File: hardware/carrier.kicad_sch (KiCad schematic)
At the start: 49 parts, among them J2 Heltec_J2, J3 Heltec_J3, U1 MT3608

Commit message: hardware: gen_sch net classes load in KiCad 9, respect lib in_bom
KiCad 9 silently drops every net class whose JSON lacks "priority", so the
Power class never reached pcbnew/DRC. MountingHole symbols are in_bom=no in
the library; keep that so footprint/symbol BOM flags match (parity).

Co-Authored-By: Claude Opus 5.5 <noreply@anthropic.com>
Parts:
- H1, H2, H3, H4: now left out of the parts list
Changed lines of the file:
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@@
 		(unit 1)
 		(exclude_from_sim no)
-		(in_bom yes)
+		(in_bom no)
 		(on_board yes)
 		(dnp no)
@@
 		(unit 1)
 		(exclude_from_sim no)
-		(in_bom yes)
+		(in_bom no)
 		(on_board yes)
 		(dnp no)
@@
 		(unit 1)
 		(exclude_from_sim no)
-		(in_bom yes)
+		(in_bom no)
 		(on_board yes)
 		(dnp no)
@@
 		(unit 1)
 		(exclude_from_sim no)
-		(in_bom yes)
+		(in_bom no)
 		(on_board yes)
 		(dnp no)

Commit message: hardware: JLCPCB assembly BOM + CPL (full SMD+THT)
design.py: LCSC map keyed by (value, footprint); check() fails if an
assembled part (not DNP, not a mounting hole) has no LCSC number or an
entry is unused. Part numbers verified live against JLCPCB's parts API
on 2026-09-29. Cap values now state the picked parts' ratings:
22uF 25V, 220uF 16V, 100uF 25V.

jlc.py (run by make fab) writes fab/jlc_bom.csv and fab/jlc_cpl.csv from
design.py and kicad-cli's pos export, and checks: BOM and CPL designators
match exactly once, every row has an LCSC number, the pos anchors equal
the board coordinates with Y negated (the Gerber convention), and every
placement lies inside the Gerber Edge.Cuts extent. Mid X/Y is the pad
centre, because THT footprints are anchored on pin 1. No rotation
offsets: ORDERING.md lists the parts to check in JLC's 3D preview.

ORDERING.md: Economic PCBA section (upload steps, THT, setup-fee types,
preview checks, stock and backups).

Co-Authored-By: Claude Opus 5.5 <noreply@anthropic.com>
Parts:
- C_BULK1: value 220uF 10V -> 220uF 16V
- C_IN1, C_OUT1, C_OUT2: value 22uF 10V -> 22uF 25V
- C_NFC1: value 100uF 10V -> 100uF 25V
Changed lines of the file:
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@@
 			)
 		)
-		(property "Value" "22uF 10V"
+		(property "Value" "22uF 25V"
 			(at 153.035 101.6 0)
 			(effects
@@
 			)
 		)
-		(property "Value" "22uF 10V"
+		(property "Value" "22uF 25V"
 			(at 168.275 96.52 0)
 			(effects
@@
 			)
 		)
-		(property "Value" "22uF 10V"
+		(property "Value" "22uF 25V"
 			(at 183.515 96.52 0)
 			(effects
@@
 			)
 		)
-		(property "Value" "220uF 10V"
+		(property "Value" "220uF 16V"
 			(at 201.295 101.6 0)
 			(effects
@@
 			)
 		)
-		(property "Value" "100uF 10V"
+		(property "Value" "100uF 25V"
 			(at 33.655 142.24 0)
 			(effects

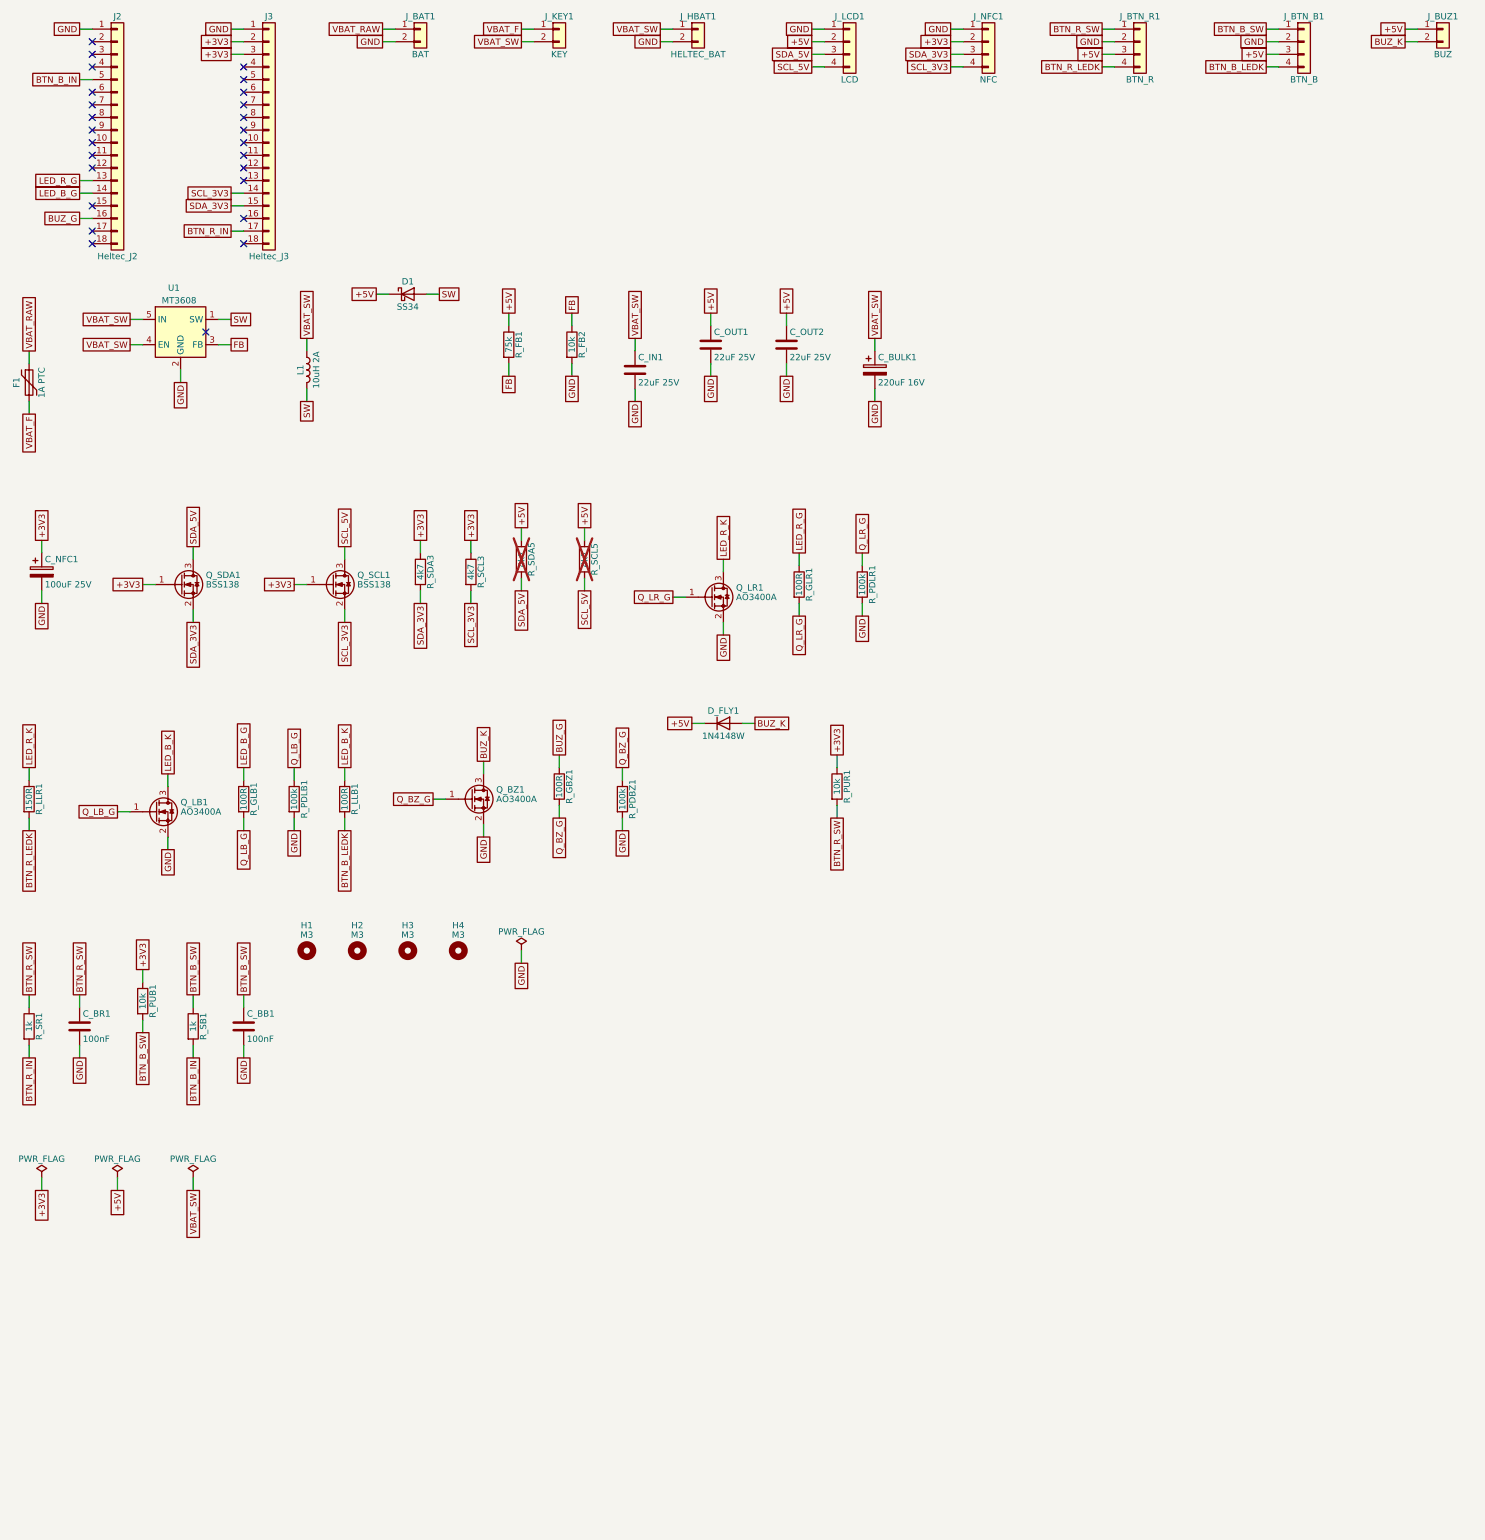
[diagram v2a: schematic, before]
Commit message: hardware: I2S speaker amp, TCA9534 expander, ceramic bulk caps
Task A10 (design Part 6):
- U2 TCA9534PWR (C783615) at 0x20 on the 3V3 I2C bus, INT on GPIO6
  (R_INT1 10k): buttons on P0/P1, LED/buzzer gate drives on P2-P4,
  amp SD_MODE on P5 (through R_SD1 1k, datasheet abs-max guidance).
- U3 MAX98357AETE+T (C910544) on VBAT_SW, I2S on GPIO47/48/21, 12 dB,
  BTL output to J_SPK1 (pin 1 OUT-, silk "SPK (BTL, not GND)").
- THT 220uF/100uF -> 2x 47uF 10V (C96123) + 100uF 6.3V (C15008) 1206
  Basic ceramics; F1 -> 2A PTC 1206L200/16NR (C22374899).
- R_LLR1/R_LLB1 -> 0R (C17477): ONPOW 6V button LEDs have a resistor.
- GND leaves the Power net class, Power clearance 0.2 mm, board min
  track 0.15 mm (Freerouting necks into the fine-pitch pads); U3
  thermal vias widened to 0.3 mm; ERC treats Unspecified as Passive.
LCSC numbers verified live 2026-09-29. ERC 0, DRC 0/0/0 at all
severities, 23 JLC BOM lines, 52 placements, deterministic rebuild.

Co-Authored-By: Claude Opus 5.5 <noreply@anthropic.com>
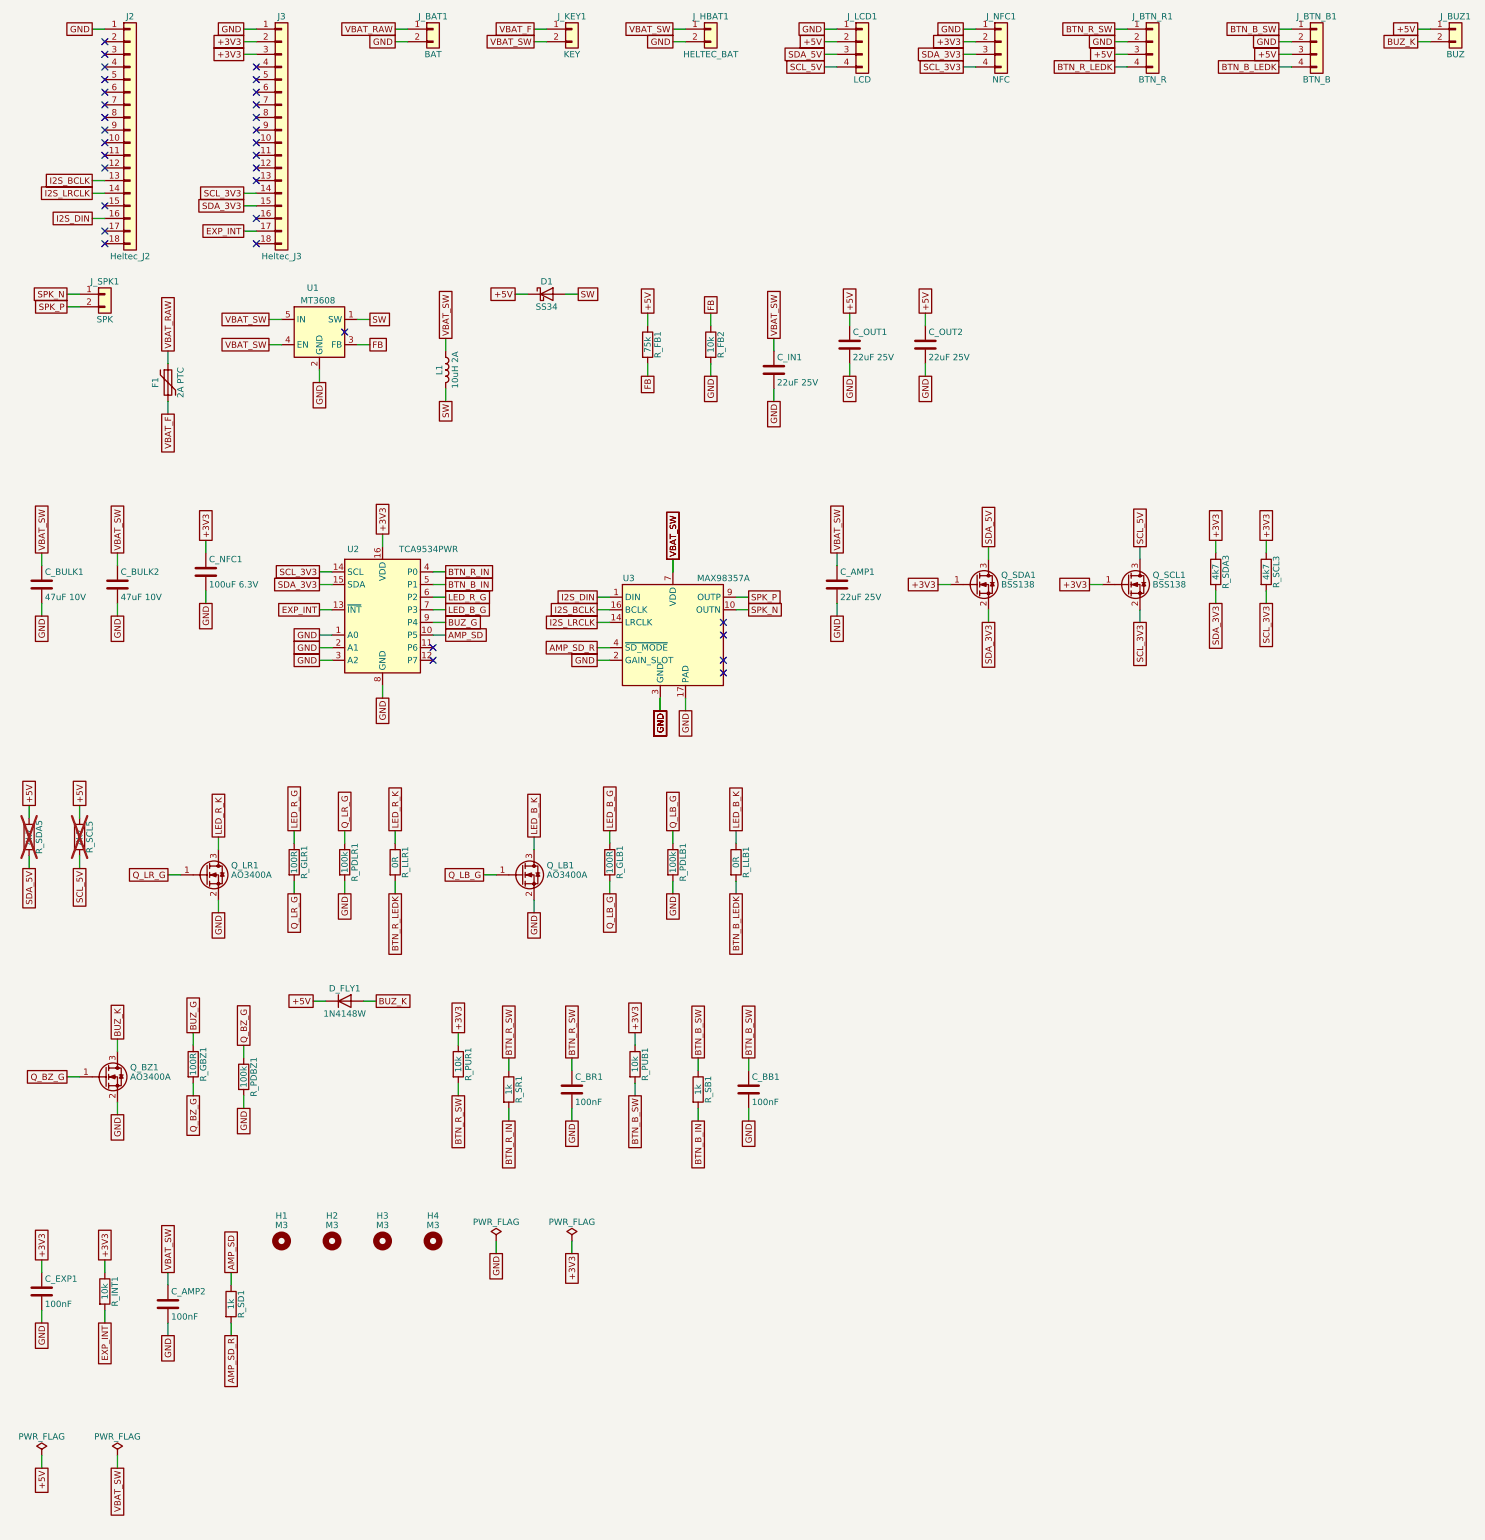
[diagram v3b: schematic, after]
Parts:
- added C_AMP1: 22uF 25V, Capacitor_SMD:C_1206_3216Metric_Pad1.33x1.80mm_HandSolder, symbol Device:C
- added C_AMP2, C_EXP1: 100nF, Capacitor_SMD:C_0805_2012Metric_Pad1.18x1.45mm_HandSolder, symbol Device:C
- added C_BULK2: 47uF 10V, Capacitor_SMD:C_1206_3216Metric_Pad1.33x1.80mm_HandSolder, symbol Device:C
- added J_SPK1: SPK, Connector_JST:JST_XH_B2B-XH-A_1x02_P2.50mm_Vertical, symbol Connector_Generic:Conn_01x02
- added R_INT1: 10k, Resistor_SMD:R_0805_2012Metric_Pad1.20x1.40mm_HandSolder, symbol Device:R
- added R_SD1: 1k, Resistor_SMD:R_0805_2012Metric_Pad1.20x1.40mm_HandSolder, symbol Device:R
- added U2: TCA9534PWR, Package_SO:TSSOP-16_4.4x5mm_P0.65mm, symbol Interface_Expansion:TCA9534
- added U3: MAX98357A, Package_DFN_QFN:TQFN-16-1EP_3x3mm_P0.5mm_EP1.23x1.23mm_ThermalVias, symbol Audio:MAX98357A
- C_BULK1: value 220uF 16V -> 47uF 10V; footprint Capacitor_THT:CP_Radial_D6.3mm_P2.50mm -> Capacitor_SMD:C_1206_3216Metric_Pad1.33x1.80mm_HandSolder; symbol Device:C_Polarized -> Device:C
- C_NFC1: value 100uF 25V -> 100uF 6.3V; footprint Capacitor_THT:CP_Radial_D6.3mm_P2.50mm -> Capacitor_SMD:C_1206_3216Metric_Pad1.33x1.80mm_HandSolder; symbol Device:C_Polarized -> Device:C
- F1: value 1A PTC -> 2A PTC
- R_LLB1: value 100R -> 0R
- R_LLR1: value 150R -> 0R
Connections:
- net +3V3: now also C_EXP1.1, R_INT1.1, U2.16 (VDD)
- net BTN_B_IN: now also U2.5 (P1); no longer J2.5 (Pin_5)
- net BTN_R_IN: now also U2.4 (P0); no longer J3.17 (Pin_17)
- net BUZ_G: now also U2.9 (P4); no longer J2.16 (Pin_16)
- net GND: now also C_AMP1.2, C_AMP2.2, C_BULK2.2, C_EXP1.2, U2.1 (A0), U2.2 (A1), U2.3 (A2), U2.8 (GND), U3.11 (GND), U3.15 (GND), U3.17 (PAD), U3.2 (GAIN_SLOT), U3.3 (GND)
- net LED_B_G: now also U2.7 (P3); no longer J2.14 (Pin_14)
- net LED_R_G: now also U2.6 (P2); no longer J2.13 (Pin_13)
- net SCL_3V3: now also U2.14 (SCL)
- net SDA_3V3: now also U2.15 (SDA)
- net VBAT_SW: now also C_AMP1.1, C_AMP2.1, C_BULK2.1, U3.7 (VDD), U3.8 (VDD)
- new net AMP_SD: R_SD1.1, U2.10 (P5)
- new net AMP_SD_R: R_SD1.2, U3.4 (~{SD_MODE})
- new net EXP_INT: J3.17 (Pin_17), R_INT1.2, U2.13 (~{INT})
- new net I2S_BCLK: J2.13 (Pin_13), U3.16 (BCLK)
- new net I2S_DIN: J2.16 (Pin_16), U3.1 (DIN)
- new net I2S_LRCLK: J2.14 (Pin_14), U3.14 (LRCLK)
- new net SPK_N: J_SPK1.1 (Pin_1), U3.10 (OUTN)
- new net SPK_P: J_SPK1.2 (Pin_2), U3.9 (OUTP)
- no-connect marks 26 -> 33
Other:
- moved on the sheet: C_BB1, C_BR1, C_IN1, C_OUT1, C_OUT2, D1, D_FLY1, F1, H1, H2, H3, H4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
